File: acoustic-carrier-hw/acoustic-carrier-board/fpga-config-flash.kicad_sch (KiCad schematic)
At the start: 22 parts, among them IC1 ECP5-BGA256, J701 Conn_02x07_Odd_Even, J702 Conn_02x09_Odd_Even, J703 Conn_02x06_Odd_Even, J704 Conn_02x06_Odd_Even, U701 W25Q128JVS, U702 W25Q128JVS

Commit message: [carrier] Redid routing to PMOD SPI-flash ah (next) add second PMOD-connector and third connector meant for PWM signalling to power board
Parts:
- removed J701: Conn_02x07_Odd_Even, Connector_PinSocket_2.54mm:PinSocket_2x07_P2.54mm_Vertical, symbol Connector_Generic:Conn_02x07_Odd_Even
- removed J702: Conn_02x09_Odd_Even, Connector_PinSocket_2.54mm:PinSocket_2x09_P2.54mm_Vertical, symbol Connector_Generic:Conn_02x09_Odd_Even
- removed J703, J704: Conn_02x06_Odd_Even, Connector_PinHeader_2.54mm:PinHeader_2x06_P2.54mm_Horizontal, symbol Connector_Generic:Conn_02x06_Odd_Even
- removed R701, R702, R703: 4.7k, Resistor_SMD:R_0402_1005Metric, symbol Device:R_Small
- removed RN701, RN702: 4x4k7, Resistor_SMD:R_Array_Convex_4x0603, symbol Device:R_Pack04
- added J701: Conn_02x03_Odd_Even, Connector_PinSocket_2.54mm:PinSocket_2x03_P2.54mm_Vertical, symbol Connector_Generic:Conn_02x03_Odd_Even
- added J702: PMOD_JTAG, iw-connector:PMOD_Pinsocket, symbol iw-connector:PMOD_JTAG
- added J703: PMOD_SPI, iw-connector:PMOD_Pinsocket, symbol iw-connector:PMOD_SPI
- added R705, R707: 4.7k, Resistor_SMD:R_0402_1005Metric, symbol Device:R_Small
- added R706: 1k, Resistor_SMD:R_0402_1005Metric, symbol Device:R_Small
- added RN707: 4x10k, Resistor_SMD:R_Array_Convex_4x0603, symbol Device:R_Pack04
- added RN708: 4x4k7, Resistor_SMD:R_Array_Convex_4x0603, symbol Device:R_Pack04
- R704: value 1k -> 4.7k; LPN C11702 -> C25900; MPN 0402WGF1001TCE -> 0402WGF4701TCE
- RN703: value 4x10k -> 4x4k7; LPN C29718 -> C1980; MPN 4D03WGJ0103T5E -> 4D03WGJ0472T5E
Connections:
- net FPGA_ADC_LED0: now also J701.5 (Pin_5)
- net FPGA_ADC_LED1: now also J701.3 (Pin_3)
- net FPGA_CFG0: now also J702.10 (IO8), R705.1
- net FPGA_CFG1: now also RN704.1 (R1.1), J702.9 (IO7)
- net FPGA_CFG2: now also J702.8 (IO6), R707.2
- net FPGA_DONE: now also RN704.2 (R2.1), J701.2 (Pin_2)
- net FPGA_RESET: now also RN704.4 (R4.1), J701.6 (Pin_6), J702.7 (IO5)
- net GND: now also R704.2, J701.1 (Pin_1), J702.11 (GND), J702.5 (GND), J703.11 (GND), J703.5 (GND), R705.2, R707.1
- net JTAG.TCK: now also R704.1, J702.4 (IO4/TCK)
- net JTAG.TDI: now also RN703.2 (R2.1), J702.2 (IO2/TDI)
- net JTAG.TDO: now also RN703.3 (R3.1), J702.3 (IO3/TDO)
- net JTAG.TMS: now also RN703.1 (R1.1), J702.1 (IO1/TMS)
- net QSPI.CSPPIn1: now also J703.1 (CSn), RN708.3 (R3.1); no longer RN703.3 (R3.1)
- net QSPI.CSPPIn2: now also J703.7 (IO1), RN708.1 (R1.1); no longer RN703.4 (R4.1)
- net QSPI.CSn: now also J703.8 (IO2), RN708.4 (R4.1)
- net QSPI.D0: now also J703.2 (MOSI/DQ0), RN707.1 (R1.1); no longer RN703.1 (R1.1)
- net QSPI.D1: now also J703.3 (MISO/DQ1), RN707.2 (R2.1); no longer RN704.4 (R4.1)
- net QSPI.D2: now also J703.9 (W/DQ2), RN707.3 (R3.1); no longer RN704.3 (R3.1)
- net QSPI.D3: now also J703.10 (HLD/DQ3), RN707.4 (R4.1); no longer RN704.1 (R1.1)
- net QSPI.MCLK: now also J703.4 (SCK), R706.2; no longer RN703.2 (R2.1)
- net VCORE_3V3: now also RN704.7 (R2.2), J702.12 (Vcc), J702.6 (Vcc), J703.12 (Vcc), J703.6 (Vcc), R706.1, RN707.5 (R4.2), RN707.6 (R3.2), RN707.7 (R2.2), RN707.8 (R1.2), RN708.5 (R4.2), RN708.6 (R3.2), RN708.8 (R1.2); no longer R704.1, RN703.5 (R4.2)
- net ~{FPGA_INIT}: now also RN704.3 (R3.1), J701.4 (Pin_4)
- no-connect marks 17 -> 8
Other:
- moved on the sheet: C704, C705, C706, C707, U701, U702

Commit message: [carrier] Routed 6x2 IO connector
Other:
- note removed: "similar component to orange-crab - nCS should be pulled low by master (FPGA) Consider using 1 Gbit in case you'd want to load firmware onto the device."
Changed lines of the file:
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@@
 	(generator_version "9.0")
 	(paper "A3")
-	(bus_alias "FLASH_MSPI"
-		(members "D[0..3]" "CSn" "CSPPIn1" "CSPPIn2" "MCLK")
-	)
-	(bus_alias "JTAG"
-		(members "TMS" "TCK" "TDI" "TDO")
-	)
 	(rectangle
 		(start 317.246 120.65)
@@
 		)
 	)
-	(text "similar component to orange-crab\n- nCS should be pulled low by master (FPGA)\n\nConsider using 1 Gbit in case you'd want to load firmware onto the device."
-		(exclude_from_sim no)
-		(at 289.56 136.906 0)
-		(effects
-			(font
-				(size 1.27 1.27)
-			)
-			(justify left)
-		)
-	)
 	(text "DEFAULT => CFG[2:0] = (010) -> MSPI2\nINPUT PINS => CFG[2:0] = (001) -> SSPI"
 		(exclude_from_sim no)
-		(at 289.56 46.99 0)
+		(at 268.732 51.054 0)
 		(effects
 			(font
@@
 	(text "Pure signaling function\nFPGA_DONE: Startup sequence in prograss\nFPGA_INITn: Ready to be configured\nFPGRA_RESET: Initiates configuration sequence when asserted low"
 		(exclude_from_sim no)
-		(at 288.544 90.932 0)
+		(at 330.962 95.25 0)
 		(effects
 			(font
@@
 	(text "pullups for Master SPI (MSPI) required by\nTN1260: lattice ECP5 sysCONFIG guide section 6"
 		(exclude_from_sim no)
-		(at 223.266 113.792 0)
+		(at 64.77 195.834 0)
 		(effects
 			(font

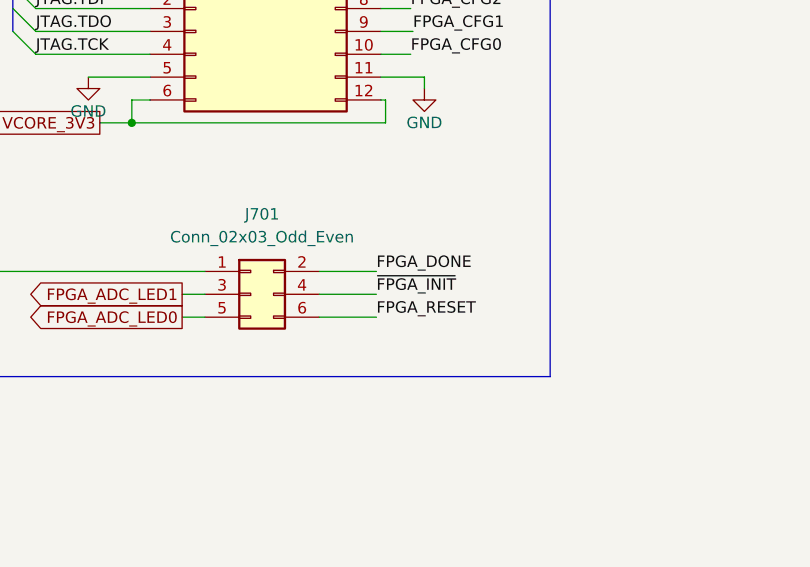
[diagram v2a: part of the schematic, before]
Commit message: [carrier] Starting on power planes
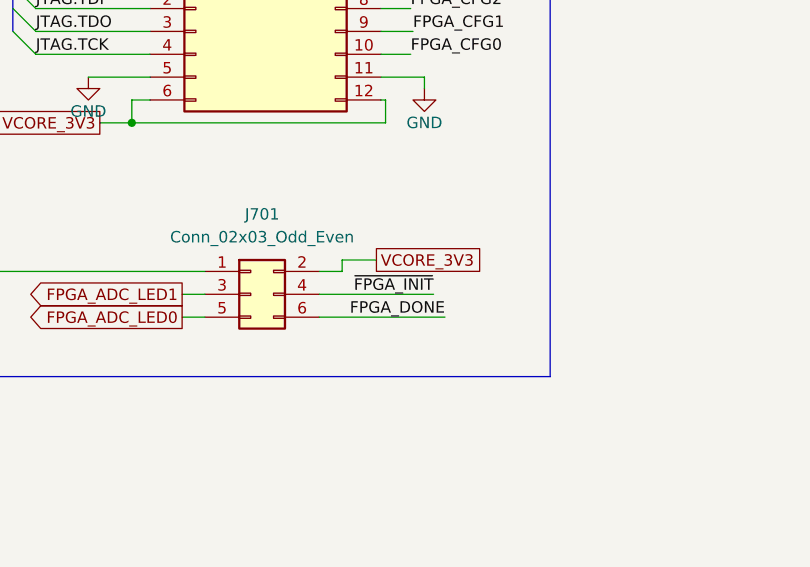
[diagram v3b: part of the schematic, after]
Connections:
- net FPGA_DONE: now also J701.6 (Pin_6); no longer J701.2 (Pin_2)
- net FPGA_RESET: no longer J701.6 (Pin_6)
- net VCORE_3V3: now also J701.2 (Pin_2)
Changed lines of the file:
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@@
+	(wire
+		(pts
+			(xy 186.69 74.93) (xy 184.15 74.93)
+		)
+		(stroke
+			(width 0)
+			(type default)
+		)
+	)
 	(wire
 		(pts
@@
 	(wire
 		(pts
-			(xy 184.15 77.47) (xy 190.5 77.47)
+			(xy 184.15 77.47) (xy 196.85 77.47)
 		)
 		(stroke
@@
 	(wire
 		(pts
-			(xy 184.15 74.93) (xy 190.5 74.93)
-		)
-		(stroke
-			(width 0)
-			(type default)
-		)
-	)
-	(wire
-		(pts
 			(xy 106.68 40.64) (xy 106.68 43.18)
 		)
@@
 	(wire
 		(pts
-			(xy 184.15 80.01) (xy 190.5 80.01)
-		)
-		(stroke
-			(width 0)
-			(type default)
-		)
-	)
-	(wire
-		(pts
 			(xy 367.03 157.48) (xy 383.54 157.48)
 		)
@@
 	(wire
 		(pts
+			(xy 184.15 80.01) (xy 198.12 80.01)
+		)
+		(stroke
+			(width 0)
+			(type default)
+		)
+	)
+	(wire
+		(pts
 			(xy 372.11 163.83) (xy 372.11 162.56)
 		)
@@
 	(wire
 		(pts
+			(xy 186.69 73.66) (xy 186.69 74.93)
+		)
+		(stroke
+			(width 0)
+			(type default)
+		)
+	)
+	(wire
+		(pts
 			(xy 199.39 133.35) (xy 204.47 133.35)
 		)
@@
 		(pts
 			(xy 260.35 132.08) (xy 266.7 132.08)
+		)
+		(stroke
+			(width 0)
+			(type default)
+		)
+	)
+	(wire
+		(pts
+			(xy 190.5 73.66) (xy 186.69 73.66)
 		)
 		(stroke
@@
 		)
 	)
+	(label "FPGA_DONE"
+		(at 198.12 80.01 180)
+		(effects
+			(font
+				(size 1.27 1.27)
+			)
+			(justify right bottom)
+		)
+	)
 	(label "~{FPGA_INIT}"
 		(at 388.62 64.77 180)
@@
 		)
 	)
-	(label "FPGA_RESET"
-		(at 190.5 80.01 0)
-		(effects
-			(font
-				(size 1.27 1.27)
-			)
-			(justify left bottom)
-		)
-	)
 	(label "QSPI.CSn"
 		(at 27.94 161.29 0)
@@
 		)
 	)
-	(label "FPGA_DONE"
-		(at 190.5 74.93 0)
-		(effects
-			(font
-				(size 1.27 1.27)
-			)
-			(justify left bottom)
-		)
-	)
 	(label "JTAG.TDI"
 		(at 67.31 72.39 0)
@@
 	)
 	(label "~{FPGA_INIT}"
-		(at 190.5 77.47 0)
-		(effects
-			(font
-				(size 1.27 1.27)
-			)
-			(justify left bottom)
+		(at 196.85 77.47 180)
+		(effects
+			(font
+				(size 1.27 1.27)
+			)
+			(justify right bottom)
 		)
 	)
@@
 				(hide yes)
 			)
+		)
+	)
+	(global_label "VCORE_3V3"
+		(shape passive)
+		(at 190.5 73.66 0)
+		(fields_autoplaced yes)
+		(effects
+			(font
+				(size 1.27 1.27)
+			)
+			(justify left)
+		)
+		(property "Intersheetrefs" "${INTERSHEET_REFS}"
+			(at 202.9572 73.66 0)
+			(effects
+				(font
+					(size 1.27 1.27)
+				)
+				(justify left)
+				(hide yes)
+			)
